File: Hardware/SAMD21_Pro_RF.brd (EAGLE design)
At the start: 44.5 x 30.5 mm, 129 parts, among them J12 JST, J13 U.FL, J7 PTH, J9 External On/Off, Q1 2.5A/30V, U1 MCP73831, U3 RFM95W, U4 ATSAMD21G, U6 3.3V, Y1 32.768kHz

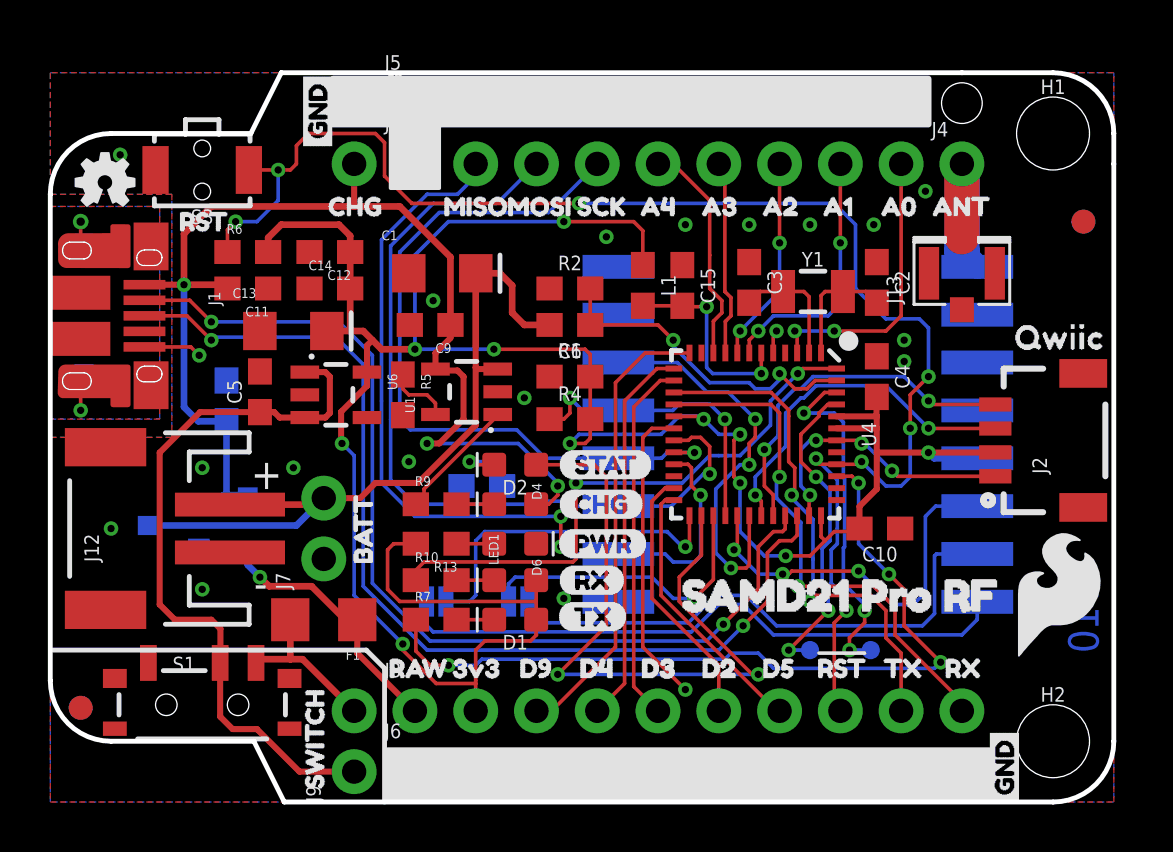
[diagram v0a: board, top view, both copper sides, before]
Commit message: v10
Cleanup of repo, updated readme.
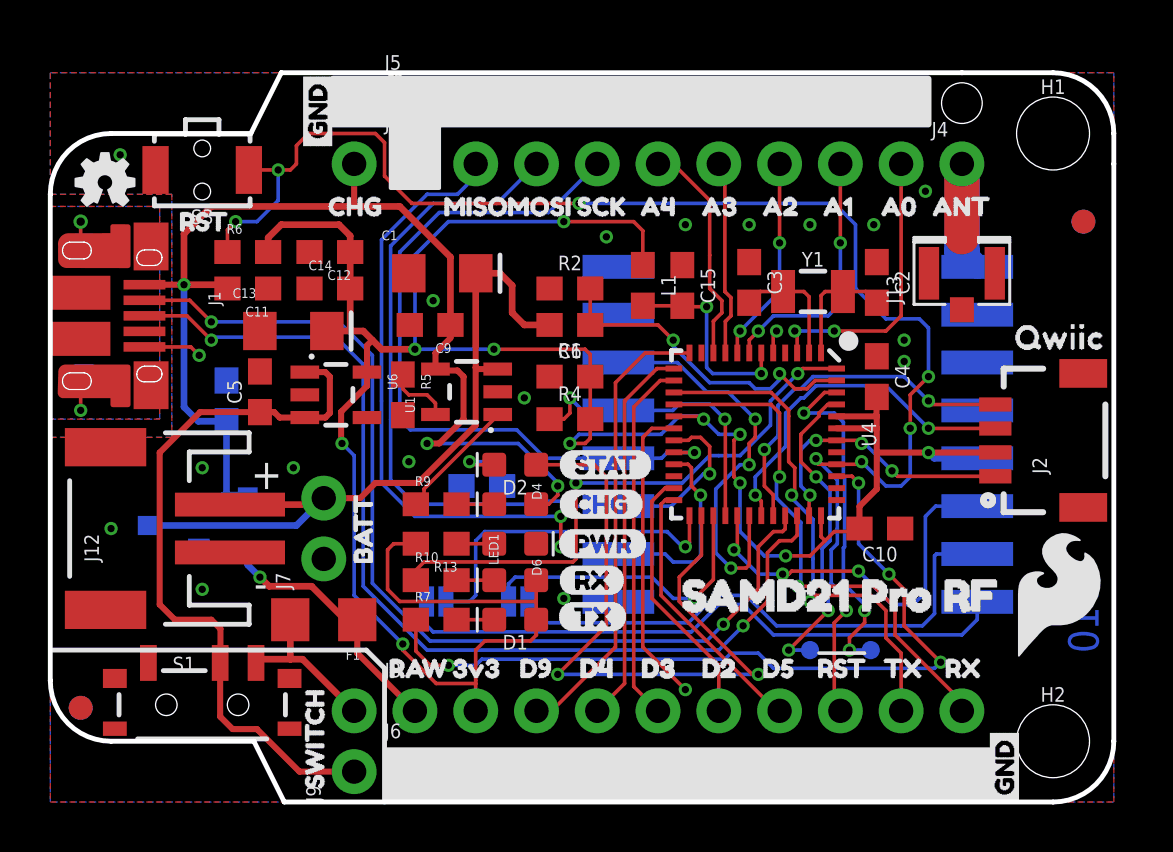
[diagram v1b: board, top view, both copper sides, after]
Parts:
- D3: value BAT20J -> 1A/23V/620mV
- Q1: device SparkFun-DiscreteSemi:SOT23-3 -> SparkFun-DiscreteSemi:SOT23-3@1
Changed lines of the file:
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@@
 <layer number="47" name="Measures" color="7" fill="1" visible="no" active="yes"/>
 <layer number="48" name="Document" color="7" fill="1" visible="no" active="yes"/>
-<layer number="49" name="Reference" color="13" fill="1" visible="no" active="yes"/>
+<layer number="49" name="Reference" color="13" fill="1" visible="yes" active="yes"/>
 <layer number="50" name="dxf" color="7" fill="1" visible="no" active="yes"/>
 <layer number="51" name="tDocu" color="6" fill="1" visible="yes" active="yes"/>
@@
 </class>
 </classes>
-<designrules name="SparkFun-2-layer-PCBWay-LIMIT">
-<description language="en">&lt;b&gt;SparkFun 2 Layer Design Rule Checks - Limits for PCBWay&lt;/b&gt;
+<designrules name="SparkFun-2-layer-FAB-LIMIT">
+<description language="en">&lt;b&gt;SparkFun 2 Layer Design Rule Checks - STANDARD/TIGHT/FAB-LIMIT&lt;/b&gt;
 &lt;p&gt;
- If you're ordering from PCBWay, these are the 'free' minimums.</description>
+These rules have been curated by SparkFuns DFM commitee. After doing much research, communicating with our multiple fab houses, and getting quotes of various designs, we have compiled three DRU files.
+&lt;p&gt;
+&lt;b&gt;STANDARD:&lt;/b&gt; This is more of a &quot;best case scenario&quot; set of limitations. If your design has the space, and/or you have the time to work within these parameters, please do. Larger trace width and clearance makes for easier visual inspection of the PCB while troubleshooting (useful in production and to the end user). It also allows for better ability to hack a trace (if you are crazy enough to scrape away the mask and solder to a trace). Another thing to keep in mind is that more metal is just more robust.
+&lt;p&gt;
+&lt;b&gt;TIGHT:&lt;/b&gt; This is where cost comes into play. We have found that most fab houses begin to add extra charges when you go smaller than these specs. In some cases, going to less than 15 mil trace can increase the cost by 10%. (This is why we have set the min drill on this DRU to 15 mil) Same story for traces thinner than 7 mil. To avoid those extra charges, then stay within the rules of this DRU.
+&lt;p&gt;
+&lt;b&gt;FAB-LIMIT:&lt;/b&gt; These set of rules are at the very limit of most fab houses capabilities. You will pay more for these specs, and it should be used on designs that have a darned good reason to need 4 mil vias and 4 mil traces.
+&lt;p&gt;
+**NOTE Clearance, Distance, Sizes, and Restring are all set to different limits in each of these three DRU files. Please compare the files within the CAM job editor window of eagle to see all the numbers.
+&lt;p&gt;
+***NOTE, Please set your Net Classes to default (0mil for all settings), so that it won't effect the DRC when you run it with these settings.</description>
 <param name="layerSetup" value="(1*16)"/>
 <param name="mtCopper" value="0.035mm 0.035mm 0.035mm 0.035mm 0.035mm 0.035mm 0.035mm 0.035mm 0.035mm 0.035mm 0.035mm 0.035mm 0.035mm 0.035mm 0.035mm 0.035mm"/>
 <param name="mtIsolate" value="1.5mm 0.15mm 0.2mm 0.15mm 0.2mm 0.15mm 0.2mm 0.15mm 0.2mm 0.15mm 0.2mm 0.15mm 0.2mm 0.15mm 0.2mm"/>
-<param name="mdWireWire" value="6mil"/>
-<param name="mdWirePad" value="6mil"/>
-<param name="mdWireVia" value="6mil"/>
-<param name="mdPadPad" value="6mil"/>
-<param name="mdPadVia" value="6mil"/>
-<param name="mdViaVia" value="6mil"/>
-<param name="mdSmdPad" value="6mil"/>
-<param name="mdSmdVia" value="6mil"/>
-<param name="mdSmdSmd" value="6mil"/>
+<param name="mdWireWire" value="4mil"/>
+<param name="mdWirePad" value="4mil"/>
+<param name="mdWireVia" value="4mil"/>
+<param name="mdPadPad" value="4mil"/>
+<param name="mdPadVia" value="4mil"/>
+<param name="mdViaVia" value="4mil"/>
+<param name="mdSmdPad" value="4mil"/>
+<param name="mdSmdVia" value="4mil"/>
+<param name="mdSmdSmd" value="4mil"/>
 <param name="mdViaViaSameLayer" value="8mil"/>
 <param name="mnLayersViaInSmd" value="2"/>
-<param name="mdCopperDimension" value="6mil"/>
-<param name="mdDrill" value="6mil"/>
+<param name="mdCopperDimension" value="4mil"/>
+<param name="mdDrill" value="4mil"/>
 <param name="mdSmdStop" value="0mil"/>
-<param name="msWidth" value="6mil"/>
-<param name="msDrill" value="0.3mm"/>
+<param name="msWidth" value="4mil"/>
+<param name="msDrill" value="6mil"/>
 <param name="msMicroVia" value="9.99mm"/>
 <param name="msBlindViaRatio" value="0.5"/>
@@
 <param name="rvMicroViaOuter" value="0.25"/>
 <param name="rvMicroViaInner" value="0.25"/>
-<param name="rlMinPadTop" value="6mil"/>
+<param name="rlMinPadTop" value="5mil"/>
 <param name="rlMaxPadTop" value="20mil"/>
 <param name="rlMinPadInner" value="6mil"/>
 <param name="rlMaxPadInner" value="20mil"/>
-<param name="rlMinPadBottom" value="6mil"/>
+<param name="rlMinPadBottom" value="5mil"/>
 <param name="rlMaxPadBottom" value="20mil"/>
-<param name="rlMinViaOuter" value="6mil"/>
+<param name="rlMinViaOuter" value="5mil"/>
 <param name="rlMaxViaOuter" value="20mil"/>
 <param name="rlMinViaInner" value="6mil"/>
 <param name="rlMaxViaInner" value="20mil"/>
-<param name="rlMinMicroViaOuter" value="6mil"/>
+<param name="rlMinMicroViaOuter" value="4mil"/>
 <param name="rlMaxMicroViaOuter" value="20mil"/>
-<param name="rlMinMicroViaInner" value="6mil"/>
+<param name="rlMinMicroViaInner" value="4mil"/>
 <param name="rlMaxMicroViaInner" value="20mil"/>
 <param name="psTop" value="-1"/>
@@
 <element name="H2" library="SparkFun-Hardware" package="STAND-OFF-TIGHT" value="STAND-OFFTIGHT" x="41.91" y="2.54"/>
 <element name="U$51" library="SparkFun-Aesthetics" package="SFE_LOGO_FLAME_.2" value="" x="40.132" y="5.842"/>
-<element name="D3" library="SparkFun-DiscreteSemi" package="SOD-323" value="BAT20J" x="8.255" y="11.684" rot="MR90">
+<element name="D3" library="SparkFun-DiscreteSemi" package="SOD-323" value="1A/23V/620mV" x="8.255" y="11.684" rot="MR90">
 <attribute name="PROD_ID" value="DIO-11623" x="17.145" y="6.604" size="1.778" layer="28" rot="MR90" display="off"/>
 </element>
@@
 <attribute name="PROD_ID" value="RES-00824" x="-0.254" y="20.574" size="1.778" layer="28" rot="MR270" display="off"/>
 </element>
-<element name="Q1" library="SparkFun-DiscreteSemi" package="SOT23-3" value="2.5A/30V" x="5.207" y="11.557" rot="MR270">
+<element name="Q1" library="SparkFun-DiscreteSemi" package="SOT23-3@1" value="2.5A/30V" x="5.207" y="11.557" rot="MR270">
 <attribute name="PROD_ID" value="TRANS-11308" x="5.207" y="20.447" size="1.778" layer="28" rot="MR270" display="off"/>
 </element>

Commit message: VDDCORE now has 01uF cap to GND
Previously, it was incorrectly connected to VDDIN (3.3V)
-bumped version to v11
-updated gitignore
-added quiic logo
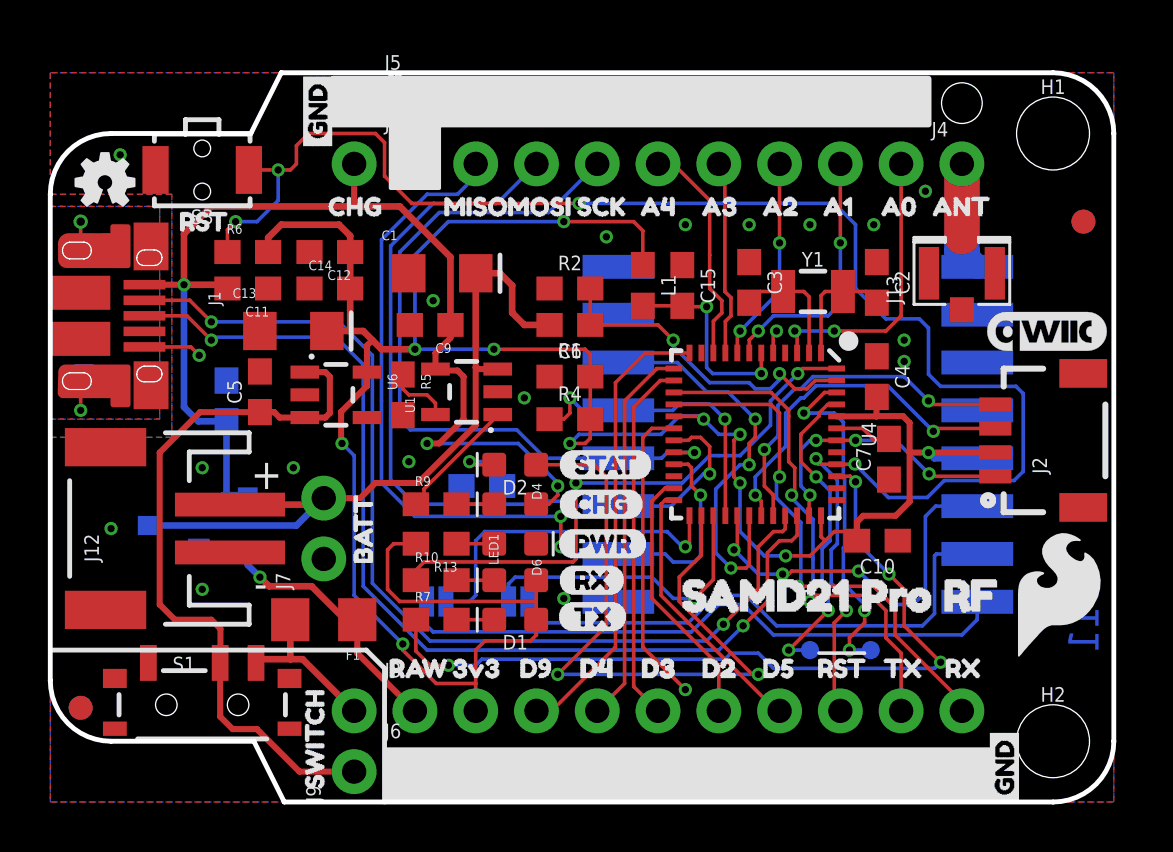
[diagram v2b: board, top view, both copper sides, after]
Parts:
- removed U$60: (no value), Labels:QWIIC-TEXT-04
- added C7: 0.1uF, SparkFun-Capacitors:0603
- added LOGO3: QWIIC_LOGO_5MM, SparkFun-Aesthetics:QWIIC_5MM
- moved U$26 4.02 mm to (-33.0, -17.8)
- moved C10 0.52 mm to (34.6, 10.9)
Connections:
- new net N$4: C7.2, U4.43
- net 3.3V: no longer U4.43
- net GND: now also C7.1
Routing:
- net !RST: track 62.9 -> 71.0 mm, vias 8 -> 6
- net N$4: track 0.00 -> 2.37 mm
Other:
- outline, holes or cut-outs redrawn
- board text added: "Pete Lewis"
- board text added: "Revised by:"
- board text added: "v11"
- board text removed: "v10"
